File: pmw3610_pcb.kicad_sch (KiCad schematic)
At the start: 23 parts, among them J1 Conn_01x06, U1 PMW3610, U2 TLV74318PDBVR

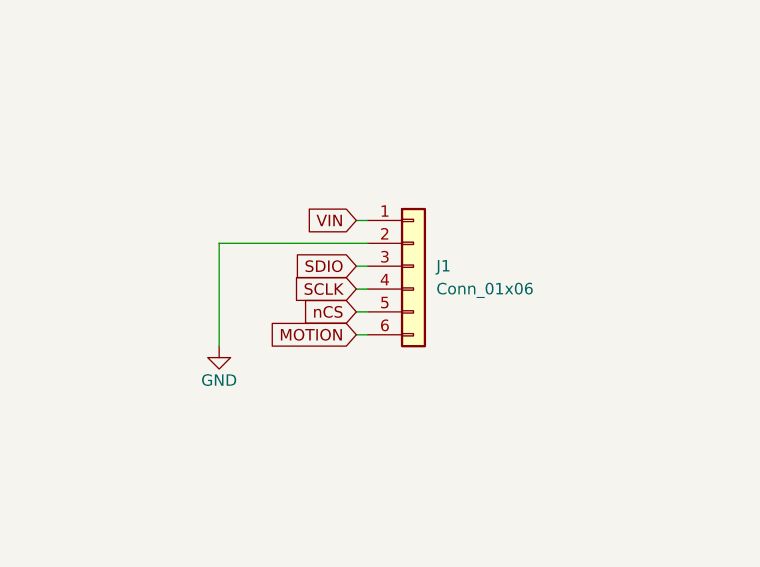
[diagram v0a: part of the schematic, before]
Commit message: Add `J2` FPC/FFC connecter
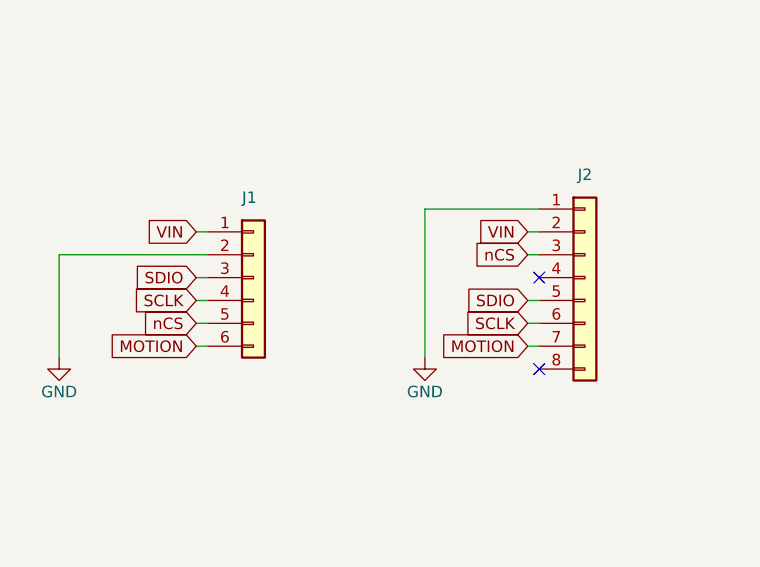
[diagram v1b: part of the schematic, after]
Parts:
- added J2: Conn_01x08, pmw3610_pcb:FPC_8P_0.5mm_AFC01-S08FCA-00, symbol Connector_Generic:Conn_01x08
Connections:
- net GND: now also J2.1 (Pin_1)
- net MOTION: now also J2.7 (Pin_7)
- net SCLK: now also J2.6 (Pin_6)
- net SDIO: now also J2.5 (Pin_5)
- net VIN: now also J2.2 (Pin_2)
- net nCS: now also J2.3 (Pin_3)
- no-connect marks 0 -> 2
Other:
- moved on the sheet: J1
